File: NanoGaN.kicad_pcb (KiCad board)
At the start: 6 copper layers, 54 x 94 mm, 199 parts, among them J1 U_DC, J10 Conn_01x06, J11 Conn_01x04, J12 USB4085-GF-A, J13 Conn_01x03, J14 Conn_01x03, J2 GND, J3 Phase_U, J4 Phase_V, J5 Phase_W, J6 FTSH-107-01-L-DV-K-TR, J7 Conn_01x03, J8 Conn_01x02, J9 Conn_01x07, Q1 IGC025S08S1, Q2 IGC025S08S1, Q3 IGC025S08S1, Q4 IGC025S08S1, Q5 IGC025S08S1, Q6 IGC025S08S1, Q7 Si2302CDS, U1 STM32H723VGTx, U10 SN74LVC1G66DCKR, U11 SN74LVC1G66DCKR, U12 LMG1205YFXR, U13 BMI323, U14 AS5047P-ATST, U15 TCAN1044VDRQ1, U16 SN74LVC1G66DCKR, U17 AD8418, U18 SN74LVC1G66DCKR, U2 LMR51635XDDCR, U3 AMS1117, U4 AD8418, U5 LMG1205YFXR, U6 SN74LVC1G66DCKR, U7 SN74LVC1G66DCKR, U8 LMG1205YFXR, U9 AD8418, X1 8MHz

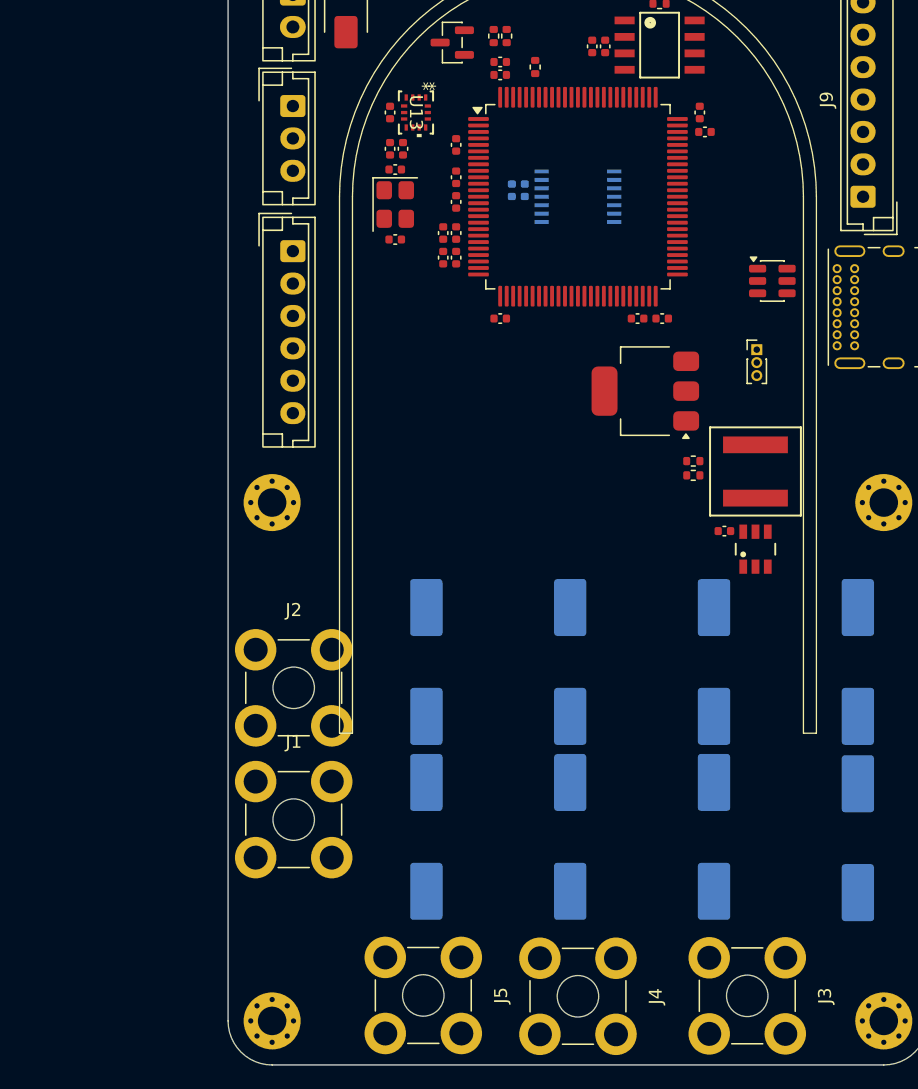
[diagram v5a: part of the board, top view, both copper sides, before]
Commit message: added over current protection triggers (adjustable)
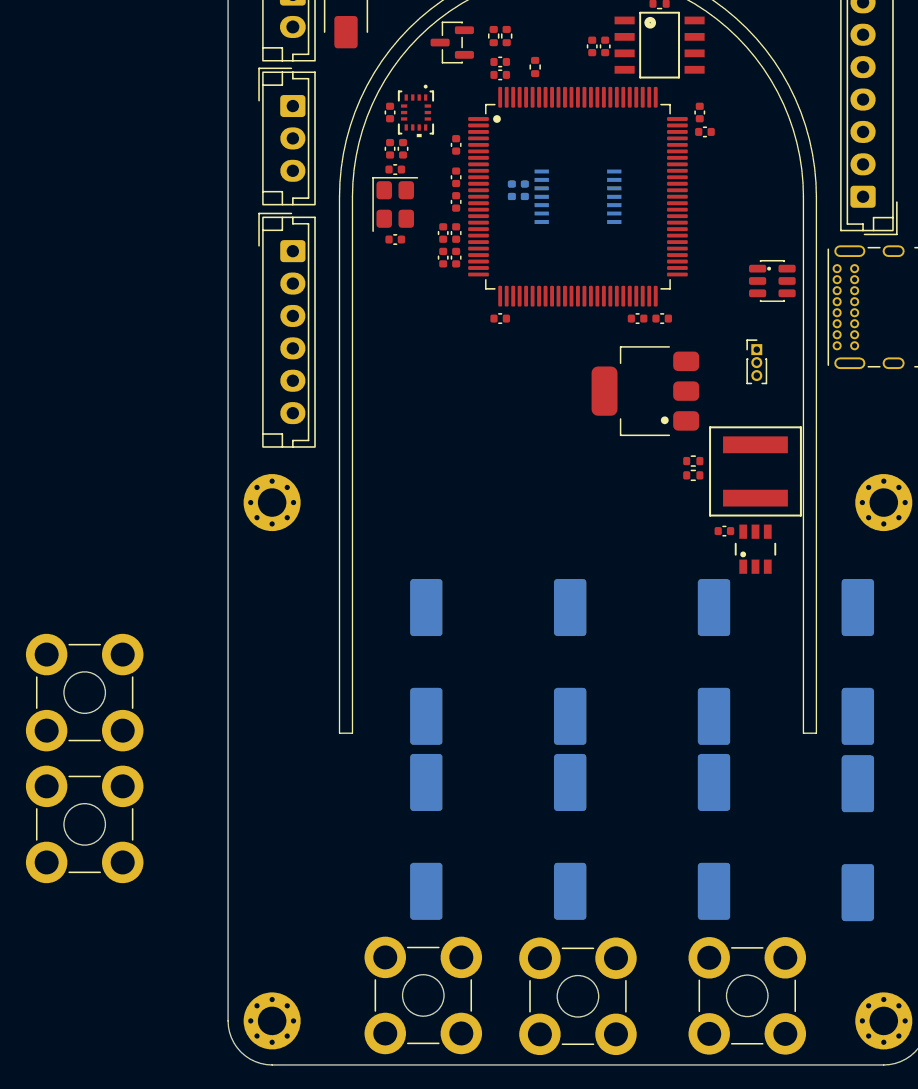
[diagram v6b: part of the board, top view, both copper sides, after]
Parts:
- moved J1 16.1 mm to (107.1, 123.4)
- moved J2 16.1 mm to (107.1, 113.3)
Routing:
- added copper zone on In1.Cu, net PGND
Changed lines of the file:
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@@
 			(layer "F.SilkS")
 		)
-		(fp_poly
-			(pts
-				(xy -7.75 -6.41) (xy -8.09 -6.88) (xy -7.41 -6.88)
-			)
+		(fp_circle
+			(center -6.25 -6)
+			(end -6 -6)
 			(stroke
-				(width 0.12)
+				(width 0.1)
 				(type solid)
 			)
@@
 			(unlocked yes)
 			(layer "F.SilkS")
+			(hide yes)
 			(effects
 				(font
@@
 		)
 		(property "Datasheet" "BMI323"
-			(at 0 0 270)
+			(at 0 0 90)
 			(layer "F.Fab")
 			(hide yes)
@@
 		)
 		(property "Description" "-40℃~+85℃ Accelerometer Gyroscope LGA-14 Accelerometers ROHS"
-			(at 0 0 270)
+			(at 0 0 90)
 			(layer "F.Fab")
 			(hide yes)
@@
 			(layer "F.SilkS")
 		)
+		(fp_circle
+			(center -2 -0.75)
+			(end -1.9 -0.75)
+			(stroke
+				(width 0.1)
+				(type solid)
+			)
+			(fill yes)
+			(layer "F.SilkS")
+		)
 		(fp_poly
 			(pts
@@
 			(layer "F.Fab")
 		)
-		(fp_text user "*"
-			(at -2.032 -1 270)
-			(unlocked yes)
-			(layer "F.SilkS")
-			(effects
-				(font
-					(size 1 1)
-					(thickness 0.15)
-				)
-			)
-		)
-		(fp_text user "*"
-			(at -2.032 -1 270)
-			(layer "F.SilkS")
-			(effects
-				(font
-					(size 1 1)
-					(thickness 0.15)
-				)
-			)
-		)
-		(fp_text user "*"
-			(at -0.9144 -1 270)
-			(unlocked yes)
-			(layer "F.Fab")
-			(effects
-				(font
-					(size 1 1)
-					(thickness 0.15)
-				)
-			)
-		)
 		(fp_text user "${REFERENCE}"
 			(at 0 0 270)
@@
 		)
 		(fp_text user "*"
-			(at -0.9144 -1 270)
+			(at -0.9144 -1 90)
 			(layer "F.Fab")
 			(effects
@@
 			(at 0 -6 90)
 			(layer "F.SilkS")
+			(hide yes)
 			(effects
 				(font
@@
 			(at 0 6 90)
 			(layer "F.Fab")
+			(hide yes)
 			(effects
 				(font
@@
 			(layer "F.SilkS")
 		)
-		(fp_poly
-			(pts
-				(xy -1.45 -1.51) (xy -1.69 -1.84) (xy -1.21 -1.84)
-			)
+		(fp_circle
+			(center -0.25 -0.95)
+			(end -0.15 -0.95)
 			(stroke
-				(width 0.12)
+				(width 0.1)
 				(type solid)
 			)
@@
 			(at 0 -6 90)
 			(layer "F.SilkS")
+			(hide yes)
 			(effects
 				(font
@@
 			(at 0 6 90)
 			(layer "F.Fab")
+			(hide yes)
 			(effects
 				(font
@@
 	(footprint "TerminalBlock_Wuerth:Wuerth_REDCUBE-THR_WP-THRBU_74650073_THR"
 		(layer "F.Cu")
-		(at 123.2301 123.065)
+		(at 107.1001 123.435)
 		(descr "REDCUBE THR with internal through-hole thread WP-THRBU (https://www.we-online.de/katalog/datasheet/74650073.pdf)")
 		(tags "screw terminal thread redcube thr power connector")
@@
 			(at 0 -6 0)
 			(layer "F.SilkS")
+			(hide yes)
 			(effects
 				(font
@@
 			(at 0 6 0)
 			(layer "F.Fab")
+			(hide yes)
 			(effects
 				(font
@@
 	(footprint "TerminalBlock_Wuerth:Wuerth_REDCUBE-THR_WP-THRBU_74650073_THR"
 		(layer "F.Cu")
-		(at 123.2301 112.895)
+		(at 107.1001 113.265)
 		(descr "REDCUBE THR with internal through-hole thread WP-THRBU (https://www.we-online.de/katalog/datasheet/74650073.pdf)")
 		(tags "screw terminal thread redcube thr power connector")
@@
 			(at 0 -6 0)
 			(layer "F.SilkS")
+			(hide yes)
 			(effects
 				(font
@@
 			(at 0 6 0)
 			(layer "F.Fab")
+			(hide yes)
 			(effects
 				(font
@@
 			(at 7.5 -2.8 90)
 			(layer "F.SilkS")
+			(hide yes)
 			(effects
 				(font
@@
 			(at 7.5 3.4 90)
 			(layer "F.Fab")
+			(hide yes)
 			(effects
 				(font
@@
 			(layer "F.SilkS")
 		)
-		(fp_poly
-			(pts
-				(xy -3.13 -3.31) (xy -3.37 -3.64) (xy -2.89 -3.64) (xy -3.13 -3.31)
-			)
+		(fp_circle
+			(center -1.5 -2.25)
+			(end -1.25 -2.25)
 			(stroke
-				(width 0.12)
+				(width 0.1)
 				(type solid)
 			)
@@
 			(at 0 -6 90)
 			(layer "F.SilkS")
+			(hide yes)
 			(effects
 				(font
@@
 			(at 0 6 90)
 			(layer "F.Fab")
+			(hide yes)
 			(effects
 				(font
@@
 		(net 138)
 	)
+	(zone
+		(net 1)
+		(net_name "PGND")
+		(layer "In1.Cu")
+		(hatch edge 0.5)
+		(connect_pads
+			(clearance 0.5)
+		)
+		(min_thickness 0.25)
+		(filled_areas_thickness no)
+		(fill
+			(thermal_gap 0.5)
+			(thermal_bridge_width 0.5)
+			(smoothing fillet)
+			(radius 1)
+		)
+		(polygon
+			(pts
+				(xy 118.1651 98.5) (xy 172.1651 98.5) (xy 172.1651 142) (xy 118.1651 142)
+			)
+		)
+	)
 	(embedded_fonts no)

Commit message: WiP layout
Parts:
- removed C67, C68: 1u, Capacitor_SMD:C_0402_1005Metric
- removed J13: Conn_01x03, Connector_PinHeader_1.00mm:PinHeader_1x03_P1.00mm_Vertical
- removed R39, R40: 0R, Resistor_SMD:R_0603_1608Metric
- added C100: 1u, Capacitor_SMD:C_0402_1005Metric, F.Cu at (215.7, 110.4)
- added C101: 100n, Capacitor_SMD:C_0402_1005Metric, F.Cu at (215.7, 112.4)
- added C102: 1u, Capacitor_SMD:C_0402_1005Metric, F.Cu at (203.9, 110.4)
- added C103: 100n, Capacitor_SMD:C_0402_1005Metric, F.Cu at (203.9, 112.4)
- added C104: 1u, Capacitor_SMD:C_0402_1005Metric, F.Cu at (203.9, 124.5)
- added C105: 100n, Capacitor_SMD:C_0402_1005Metric, F.Cu at (203.9, 126.4)
- added C94: 1n, Capacitor_SMD:C_0201_0603Metric, F.Cu at (211.4, 115.3)
- added C95: 1n, Capacitor_SMD:C_0201_0603Metric, F.Cu at (199.7, 115.3)
- added C96: 1n, Capacitor_SMD:C_0201_0603Metric, F.Cu at (199.7, 129.4)
- added C97: 1n, Capacitor_SMD:C_0201_0603Metric, F.Cu at (211.4, 117.1)
- added C98: 1n, Capacitor_SMD:C_0201_0603Metric, F.Cu at (199.7, 117.1)
- added C99: 1n, Capacitor_SMD:C_0201_0603Metric, F.Cu at (199.7, 131.1)
- added R63: 10k, Resistor_SMD:R_0402_1005Metric, F.Cu at (208.8, 118.4)
- added R64: 10k, Resistor_SMD:R_0402_1005Metric, F.Cu at (197.0, 118.4)
- added R65: 10k, Resistor_SMD:R_0402_1005Metric, F.Cu at (197.0, 132.4)
- added R66: 10k, Resistor_SMD:R_0402_1005Metric, F.Cu at (208.8, 120.4)
- added R67: 10k, Resistor_SMD:R_0402_1005Metric, F.Cu at (197.0, 120.4)
- added R68: 10k, Resistor_SMD:R_0402_1005Metric, F.Cu at (197.0, 134.4)
- added R69: 39k, Resistor_SMD:R_0603_1608Metric, F.Cu at (212.2, 110.7)
- added R70: 39k, Resistor_SMD:R_0603_1608Metric, F.Cu at (200.4, 110.7)
- added R71: 39k, Resistor_SMD:R_0603_1608Metric, F.Cu at (200.4, 124.7)
- added R72: 39k, Resistor_SMD:R_0603_1608Metric, F.Cu at (212.2, 113.2)
- added R73: 39k, Resistor_SMD:R_0603_1608Metric, F.Cu at (200.4, 113.2)
- added R74: 39k, Resistor_SMD:R_0603_1608Metric, F.Cu at (200.4, 127.2)
- added U19: NCS2220AMUT1G, NanoGaN:UDFN8_1P6X1P6_ONS, F.Cu at (214.9, 116.4)
- added U20: NCS2220AMUT1G, NanoGaN:UDFN8_1P6X1P6_ONS, F.Cu at (203.1, 116.4)
- added U21: NCS2220AMUT1G, NanoGaN:UDFN8_1P6X1P6_ONS, F.Cu at (203.1, 130.4)
- R44, R45, R46, R47, R48, R49: value 0 -> 1
- moved R28 139.2 mm to (135.2, 128.0), turned to -90 degrees
- moved C3 121.8 mm to (154.3, 109.9), turned to -90 degrees
- moved C2 121.6 mm to (156.7, 109.9), turned to -90 degrees
- moved C1 121.5 mm to (159.1, 109.9), turned to -90 degrees
- moved C4 118.4 mm to (161.4, 109.7), turned to -90 degrees
- moved U9 117.9 mm to (143.9, 128.2), turned to -90 degrees
- moved R21 112.7 mm to (148.5, 128.4), turned to 90 degrees
- moved U8 112.5 mm to (145.3, 114.2)
- moved C86 108.7 mm to (156.0, 93.3), turned to 90 degrees
- moved C82 107.6 mm to (158.5, 93.3), turned to 90 degrees
- moved C6 106.6 mm to (161.0, 93.3), turned to 90 degrees
- moved Q3 104.8 mm to (148.2, 121.1), turned to -90 degrees
- moved R15 103.8 mm to (148.7, 116.4), turned to -90 degrees
- moved Q4 103.7 mm to (143.2, 121.1), turned to -90 degrees
- moved R11 86.4 mm to (161.2, 128.0), turned to 90 degrees
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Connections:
- C6 pad 1: +5V_SMPS -> +5V
- C82 pad 1: +5V_SMPS -> +5V
- C86 pad 1: +5V_SMPS -> +5V
- D2 pad 2: GND -> unconnected-(D2-GND-Pad2)
- D2 pad 5: /Connectors/USBVBUS -> unconnected-(D2-VBUS-Pad5)
- J12 pad A4: /Connectors/USBVBUS -> unconnected-(J12-VBUS-PadA4)_1
- J12 pad A9: /Connectors/USBVBUS -> unconnected-(J12-VBUS-PadA4)_3
- J12 pad B4: /Connectors/USBVBUS -> unconnected-(J12-VBUS-PadA4)
- J12 pad B9: /Connectors/USBVBUS -> unconnected-(J12-VBUS-PadA4)_2
- L1 pad 2: +5V_SMPS -> +5V
- MH3 pad 1: GND -> PGND
- MH4 pad 1: GND -> PGND
- MH5 pad 1: GND -> PGND
- MH6 pad 1: GND -> PGND
- R1 pad 1: +5V_SMPS -> +5V
- R7 pad 2: GND -> +3V3
- U1 pad 24: /Connectors/HALL1 -> unconnected-(U1-PA2-Pad24)
- U1 pad 25: /Connectors/HALL2 -> unconnected-(U1-PA3-Pad25)
- U1 pad 28: /Connectors/HALL3 -> /HalfBridgeU/DAC_OCP_P
- U1 pad 29: unconnected-(U1-PA5-Pad29) -> /HalfBridgeU/DAC_OCP_N
- U1 pad 68: /Connectors/VBUS -> unconnected-(U1-PA9-Pad68)
